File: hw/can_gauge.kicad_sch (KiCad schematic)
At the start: 28 parts, among them J1 Gauge 1, J2 Gauge 2, J3 Gauge 3, J4 Gauge 4, J5 Gauge 5, J6 Gauge 6, J7 Power & CAN, U1 PIC16F1459-IP, U2 MCP2515-xST, U3 MCP2561T-E/SN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

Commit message: hw: partial uc layout
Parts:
- removed U2: MCP2515-xST, Package_SO:TSSOP-20_4.4x6.5mm_P0.65mm, symbol Interface_CAN_LIN:MCP2515-xST
- removed U3: MCP2561T-E/SN, Package_SO:SOIC-8_3.9x4.9mm_P1.27mm, symbol Interface_CAN_LIN:MCP2561-E-SN
- added U2: ~, Package_DIP:DIP-18_W7.62mm, symbol symbols:MCP2515-xP
- added XCVR1: MCP2561-E-P, Package_DIP:DIP-8_W7.62mm, symbol Interface_CAN_LIN:MCP2561-E-P
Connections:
- net +12V: now also J7.3 (Pin_3); no longer J7.4 (Pin_4)
- net +5V: now also U2.18 (VDD), XCVR1.3 (VDD)
- net CAN_H: now also J7.2 (Pin_2), XCVR1.7 (CANH); no longer J7.1 (Pin_1)
- net CAN_L: now also J7.4 (Pin_4), XCVR1.6 (CANL); no longer J7.3 (Pin_3)
- net CLK: now also U2.8 (OSC1)
- net GND: now also J7.1 (Pin_1), U2.9 (VSS), XCVR1.2 (VSS), XCVR1.8 (STBY); no longer J7.2 (Pin_2)
- net RX: now also U2.2 (RXCAN), XCVR1.4 (RXD)
- net SCK: now also U2.13 (SCK)
- net SI: now also U2.15 (SO)
- net SO: now also U2.14 (SI)
- net TX: now also U2.1 (TXCAN), XCVR1.1 (TXD)
- net ~{CS}: now also U2.16 (~{CS})
- net ~{INT}: now also U2.12 (~{INT})
- net at R2.1: now also U2.17 (~{RESET})
- no-connect marks 10 -> 15
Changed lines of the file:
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@@
 	)
 	(no_connect
+		(at 123.19 57.15)
+	)
+	(no_connect
 		(at 123.19 41.91)
 	)
@@
 	)
 	(no_connect
+		(at 123.19 69.85)
+	)
+	(no_connect
 		(at 66.04 66.04)
 	)
 	(no_connect
+		(at 224.79 62.23)
+	)
+	(no_connect
+		(at 224.79 46.99)
+	)
+	(no_connect
 		(at 63.5 127)
 	)
 	(no_connect
+		(at 224.79 64.77)
+	)
+	(no_connect
 		(at 278.13 204.47)
 	)
@@
 	(wire
 		(pts
+			(xy 57.15 264.16) (xy 69.85 264.16)
+		)
+		(stroke
+			(width 0)
+			(type default)
+		)
+	)
+	(wire
+		(pts
 			(xy 322.58 179.07) (xy 325.12 179.07)
 		)
@@
 	(wire
 		(pts
-			(xy 57.15 261.62) (xy 63.5 261.62)
+			(xy 248.92 123.19) (xy 248.92 186.69)
 		)
 		(stroke
@@
 	(wire
 		(pts
-			(xy 248.92 123.19) (xy 248.92 186.69)
+			(xy 30.48 261.62) (xy 44.45 261.62)
 		)
 		(stroke
@@
 	(global_label "CAN_H"
 		(shape bidirectional)
-		(at 44.45 261.62 180)
+		(at 44.45 264.16 180)
 		(fields_autoplaced yes)
 		(effects
@@
 		)
 		(property "Intersheetrefs" "${INTERSHEET_REFS}"
-			(at 34.3663 261.62 0)
+			(at 34.3663 264.16 0)
 			(effects
 				(font
@@
 	(global_label "CAN_L"
 		(shape bidirectional)
-		(at 57.15 264.16 0)
+		(at 57.15 261.62 0)
 		(fields_autoplaced yes)
 		(effects
@@
 		)
 		(property "Intersheetrefs" "${INTERSHEET_REFS}"
-			(at 66.9313 264.16 0)
+			(at 66.9313 261.62 0)
 			(effects
 				(font
@@
 	)
 	(symbol
+		(lib_id "Interface_CAN_LIN:MCP2561-E-P")
+		(at 50.8 127 0)
+		(unit 1)
+		(exclude_from_sim no)
+		(in_bom yes)
+		(on_board yes)
+		(dnp no)
+		(fields_autoplaced yes)
+		(property "Reference" "XCVR1"
+			(at 52.9433 114.3 0)
+			(effects
+				(font
+					(size 1.27 1.27)
+				)
+				(justify left)
+			)
+		)
+		(property "Value" "MCP2561-E-P"
+			(at 52.9433 116.84 0)
+			(effects
+				(font
+					(size 1.27 1.27)
+				)
+				(justify left)
+			)
+		)
+		(property "Footprint" "Package_DIP:DIP-8_W7.62mm"
+			(at 50.8 139.7 0)
+			(effects
+				(font
+					(size 1.27 1.27)
+					(italic yes)
+				)
+				(hide yes)
+			)
+		)
+		(property "Datasheet" "http://ww1.microchip.com/downloads/en/DeviceDoc/25167A.pdf"
+			(at 50.8 127 0)
+			(effects
+				(font
+					(size 1.27 1.27)
+				)
+				(hide yes)
+			)
+		)
+		(property "Description" "High-Speed CAN Transceiver, 1Mbps, 5V supply, SPLIT pin, -40C to +125C, DIP-8"
+			(at 50.8 127 0)
+			(effects
+				(font
+					(size 1.27 1.27)
+				)
+				(hide yes)
+			)
+		)
+		(pin "1"
+		)
+		(pin "5"
+		)
+		(pin "3"
+		)
+		(pin "8"
+		)
+		(pin "7"
+		)
+		(pin "6"
+		)
+		(pin "2"
+		)
+		(pin "4"
+		)
+		(instances
+			(project ""
+				(path "/a1545928-1195-40b9-b3c4-78f837012afb"
+					(reference "XCVR1")
+					(unit 1)
+				)
+			)
+		)
+	)
+	(symbol
 		(lib_name "GND_8")
 		(lib_id "power:GND")
@@
 	)
 	(symbol
-		(lib_id "Interface_CAN_LIN:MCP2515-xST")
+		(lib_id "symbols:MCP2515-xP")
 		(at 50.8 55.88 0)
 		(unit 1)
@@
 		(on_board yes)
 		(dnp no)
-		(fields_autoplaced yes)
 		(property "Reference" "U2"
-			(at 52.9433 33.02 0)
+			(at 52.324 33.782 0)
 			(effects
 				(font
@@
 			)
 		)
-		(property "Value" "MCP2515-xST"
-			(at 52.9433 35.56 0)
+		(property "Value" "~"
+			(at 52.9433 34.29 0)
 			(effects
 				(font
@@
 			)
 		)
-		(property "Footprint" "Package_SO:TSSOP-20_4.4x6.5mm_P0.65mm"
-			(at 50.8 78.74 0)
+		(property "Footprint" "Package_DIP:DIP-18_W7.62mm"
+			(at 50.8 55.88 0)
 			(effects
 				(font
 					(size 1.27 1.27)
-					(italic yes)
 				)
 				(hide yes)
 			)
 		)
-		(property "Datasheet" "http://ww1.microchip.com/downloads/en/DeviceDoc/21801e.pdf"
-			(at 53.34 76.2 0)
+		(property "Datasheet" "https://ww1.microchip.com/downloads/aemDocuments/documents/APID/ProductDocuments/DataSheets/MCP2515-Family-Data-Sheet-DS20001801K.pdf"
+			(at 50.8 55.88 0)
 			(effects
 				(font
@@
 			)
 		)
-		(property "Description" "Stand-Alone CAN Controller with SPI Interface, TSSOP-20"
+		(property "Description" "CAN transceiver with SPI interface"
 			(at 50.8 55.88 0)
 			(effects
@@
 			)
 		)
-		(pin "5"
-		)
-		(pin "18"
-		)
-		(pin "20"
-		)
-		(pin "19"
-		)
-		(pin "14"
+		(pin "9"
 		)
-		(pin "7"
+		(pin "5"
 		)
 		(pin "6"
 		)
-		(pin "10"
-		)
-		(pin "3"
+		(pin "17"
 		)
-		(pin "15"
+		(pin "10"
 		)
 		(pin "12"
 		)
+		(pin "18"
+		)
 		(pin "1"
 		)
 		(pin "4"
 		)
+		(pin "11"
+		)
 		(pin "2"
 		)
-		(pin "9"
+		(pin "8"
 		)
-		(pin "11"
+		(pin "3"
 		)
-		(pin "17"
+		(pin "7"
+		)
+		(pin "13"
 		)
 		(pin "16"
 		)
-		(pin "8"
+		(pin "14"
 		)
-		(pin "13"
+		(pin "15"
 		)
 		(instances
@@
 		(lib_name "GND_5")
 		(lib_id "power:GND")
-		(at 44.45 264.16 0)
+		(at 30.48 261.62 0)
 		(unit 1)
 		(exclude_from_sim no)
@@
 		(fields_autoplaced yes)
 		(property "Reference" "#PWR09"
-			(at 44.45 270.51 0)
+			(at 30.48 267.97 0)
 			(effects
 				(font
@@
 		)
 		(property "Value" "GND"
-			(at 44.45 269.24 0)
+			(at 30.48 266.7 0)
 			(effects
 				(font
@@
 		)
 		(property "Footprint" ""
-			(at 44.45 264.16 0)
+			(at 30.48 261.62 0)
 			(effects
 				(font
@@
 		)
 		(property "Datasheet" ""
-			(at 44.45 264.16 0)
+			(at 30.48 261.62 0)
 			(effects
 				(font
@@
 		)
 		(property "Description" "Power symbol creates a global label with name \"GND\" , ground"
-			(at 44.45 264.16 0)
+			(at 30.48 261.62 0)
 			(effects
 				(font
@@
 	)
 	(symbol
-		(lib_id "Interface_CAN_LIN:MCP2561-E-SN")
-		(at 50.8 127 0)
-		(unit 1)
-		(exclude_from_sim no)
-		(in_bom yes)
-		(on_board yes)
-		(dnp no)
-		(property "Reference" "U3"
-			(at 52.9433 114.3 0)
-			(effects
-				(font
-					(size 1.27 1.27)
-				)
-				(justify left)
-			)
-		)
-		(property "Value" "MCP2561T-E/SN"
-			(at 52.9433 116.84 0)
-			(effects
-				(font
-					(size 1.27 1.27)
-				)
-				(justify left)
-			)
-		)
-		(property "Footprint" "Package_SO:SOIC-8_3.9x4.9mm_P1.27mm"
-			(at 50.8 139.7 0)
-			(effects
-				(font
-					(size 1.27 1.27)
-					(italic yes)
-				)
-				(hide yes)
-			)
-		)
-		(property "Datasheet" "https://ww1.microchip.com/downloads/en/DeviceDoc/20005167C.pdf"
-			(at 50.8 127 0)
-			(effects
-				(font
-					(size 1.27 1.27)
-				)
-				(hide yes)
-			)
-		)
-		(property "Description" "High-Speed CAN Transceiver, 1Mbps, 5V supply, SPLIT pin, -40C to +125C, SOIC-8"
-			(at 50.8 127 0)
-			(effects
-				(font
-					(size 1.27 1.27)
-				)
-				(hide yes)
-			)
-		)
-		(pin "3"
-		)
-		(pin "5"
-		)
-		(pin "7"
-		)
-		(pin "8"
-		)
-		(pin "4"
-		)
-		(pin "1"
-		)
-		(pin "6"
-		)
-		(pin "2"
-		)
-		(instances
-			(project ""
-				(path "/a1545928-1195-40b9-b3c4-78f837012afb"
-					(reference "U3")
-					(unit 1)
-				)
-			)
-		)
-	)
-	(symbol
 		(lib_id "power:GND")
 		(at 118.11 130.81 0)
@@
 		(lib_name "+12V_1")
 		(lib_id "power:+12V")
-		(at 63.5 261.62 0)
+		(at 69.85 264.16 0)
 		(unit 1)
 		(exclude_from_sim no)
@@
 		(fields_autoplaced yes)
 		(property "Reference" "#PWR08"
-			(at 63.5 265.43 0)
+			(at 69.85 267.97 0)
 			(effects
 				(font
@@
 		)
 		(property "Value" "+12V"
-			(at 63.5 256.54 0)
+			(at 69.85 259.08 0)
 			(effects
 				(font
@@
 		)
 		(property "Footprint" ""
-			(at 63.5 261.62 0)
+			(at 69.85 264.16 0)
 			(effects
 				(font
@@
 		)
 		(property "Datasheet" ""
-			(at 63.5 261.62 0)
+			(at 69.85 264.16 0)
 			(effects
 				(font
@@
 		)
 		(property "Description" "Power symbol creates a global label with name \"+12V\""
-			(at 63.5 261.62 0)
+			(at 69.85 264.16 0)
 			(effects
 				(font

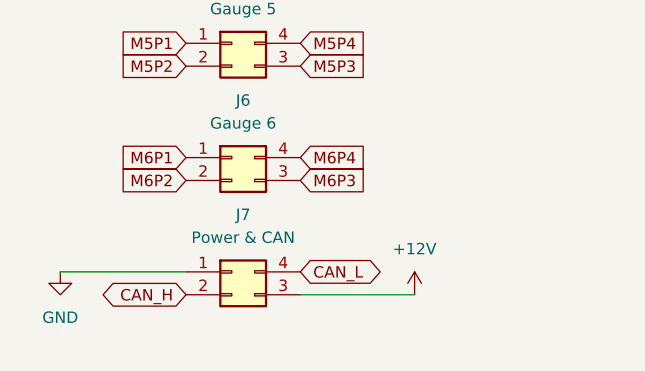
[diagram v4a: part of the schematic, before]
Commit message: hw: vreg placement
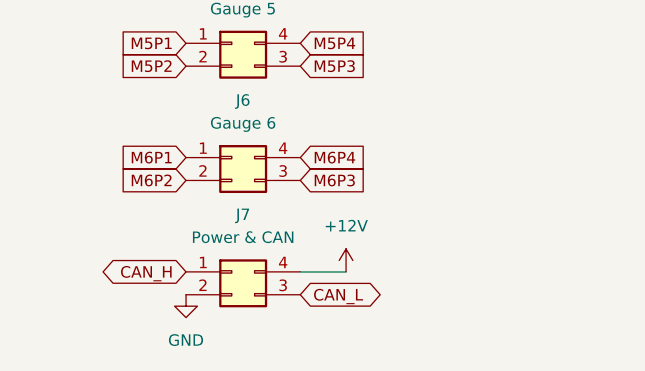
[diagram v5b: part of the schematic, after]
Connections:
- net +12V: now also J7.4 (Pin_4); no longer J7.3 (Pin_3)
- net CAN_H: now also J7.1 (Pin_1); no longer J7.2 (Pin_2)
- net CAN_L: now also J7.3 (Pin_3); no longer J7.4 (Pin_4)
- net GND: now also J7.2 (Pin_2); no longer J7.1 (Pin_1)
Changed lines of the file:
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@@
 	(wire
 		(pts
-			(xy 57.15 264.16) (xy 69.85 264.16)
-		)
-		(stroke
-			(width 0)
-			(type default)
-		)
-	)
-	(wire
-		(pts
 			(xy 322.58 179.07) (xy 325.12 179.07)
 		)
@@
 	(wire
 		(pts
-			(xy 30.48 261.62) (xy 44.45 261.62)
-		)
-		(stroke
-			(width 0)
-			(type default)
-		)
-	)
-	(wire
-		(pts
 			(xy 267.97 171.45) (xy 267.97 176.53)
 		)
@@
 	(wire
 		(pts
+			(xy 57.15 261.62) (xy 62.23 261.62)
+		)
+		(stroke
+			(width 0)
+			(type default)
+		)
+	)
+	(wire
+		(pts
 			(xy 255.27 62.23) (xy 255.27 64.77)
 		)
@@
 	(global_label "CAN_H"
 		(shape bidirectional)
-		(at 44.45 264.16 180)
+		(at 44.45 261.62 180)
 		(fields_autoplaced yes)
 		(effects
@@
 		)
 		(property "Intersheetrefs" "${INTERSHEET_REFS}"
-			(at 34.3663 264.16 0)
+			(at 34.3663 261.62 0)
 			(effects
 				(font
@@
 	(global_label "CAN_L"
 		(shape bidirectional)
-		(at 57.15 261.62 0)
+		(at 57.15 264.16 0)
 		(fields_autoplaced yes)
 		(effects
@@
 		)
 		(property "Intersheetrefs" "${INTERSHEET_REFS}"
-			(at 66.9313 261.62 0)
+			(at 66.9313 264.16 0)
 			(effects
 				(font
@@
 		(lib_name "GND_5")
 		(lib_id "power:GND")
-		(at 30.48 261.62 0)
+		(at 44.45 264.16 0)
 		(unit 1)
 		(exclude_from_sim no)
@@
 		(fields_autoplaced yes)
 		(property "Reference" "#PWR09"
-			(at 30.48 267.97 0)
+			(at 44.45 270.51 0)
 			(effects
 				(font
@@
 		)
 		(property "Value" "GND"
-			(at 30.48 266.7 0)
+			(at 44.45 269.24 0)
 			(effects
 				(font
@@
 		)
 		(property "Footprint" ""
-			(at 30.48 261.62 0)
+			(at 44.45 264.16 0)
 			(effects
 				(font
@@
 		)
 		(property "Datasheet" ""
-			(at 30.48 261.62 0)
+			(at 44.45 264.16 0)
 			(effects
 				(font
@@
 		)
 		(property "Description" "Power symbol creates a global label with name \"GND\" , ground"
-			(at 30.48 261.62 0)
+			(at 44.45 264.16 0)
 			(effects
 				(font
@@
 		(lib_name "+12V_1")
 		(lib_id "power:+12V")
-		(at 69.85 264.16 0)
+		(at 62.23 261.62 0)
 		(unit 1)
 		(exclude_from_sim no)
@@
 		(fields_autoplaced yes)
 		(property "Reference" "#PWR08"
-			(at 69.85 267.97 0)
+			(at 62.23 265.43 0)
 			(effects
 				(font
@@
 		)
 		(property "Value" "+12V"
-			(at 69.85 259.08 0)
+			(at 62.23 256.54 0)
 			(effects
 				(font
@@
 		)
 		(property "Footprint" ""
-			(at 69.85 264.16 0)
+			(at 62.23 261.62 0)
 			(effects
 				(font
@@
 		)
 		(property "Datasheet" ""
-			(at 69.85 264.16 0)
+			(at 62.23 261.62 0)
 			(effects
 				(font
@@
 		)
 		(property "Description" "Power symbol creates a global label with name \"+12V\""
-			(at 69.85 264.16 0)
+			(at 62.23 261.62 0)
 			(effects
 				(font

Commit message: hw: USB port
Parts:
- added C10: 0.1 uF, Capacitor_THT:C_Rect_L4.0mm_W2.5mm_P2.50mm, symbol Device:C_Small
- added F1: 500 mA, Fuse:Fuse_0402_1005Metric, symbol Device:Fuse_Small
- added J8: USB_B, footprints:UJ2-BH-BL1-TH, symbol Connector:USB_B
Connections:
- net +5V: now also C10.2, F1.2
- net GND: now also C10.1, J8.4 (GND), J8.5 (Shield)
- net USB+: now also U1.19 (RA0/D+/ICSPDAT), J8.3 (D+)
- net USB-: now also U1.18 (RA1/D-/ICSPCLK), J8.2 (D-)
- new net: F1.1, J8.1 (VBUS)

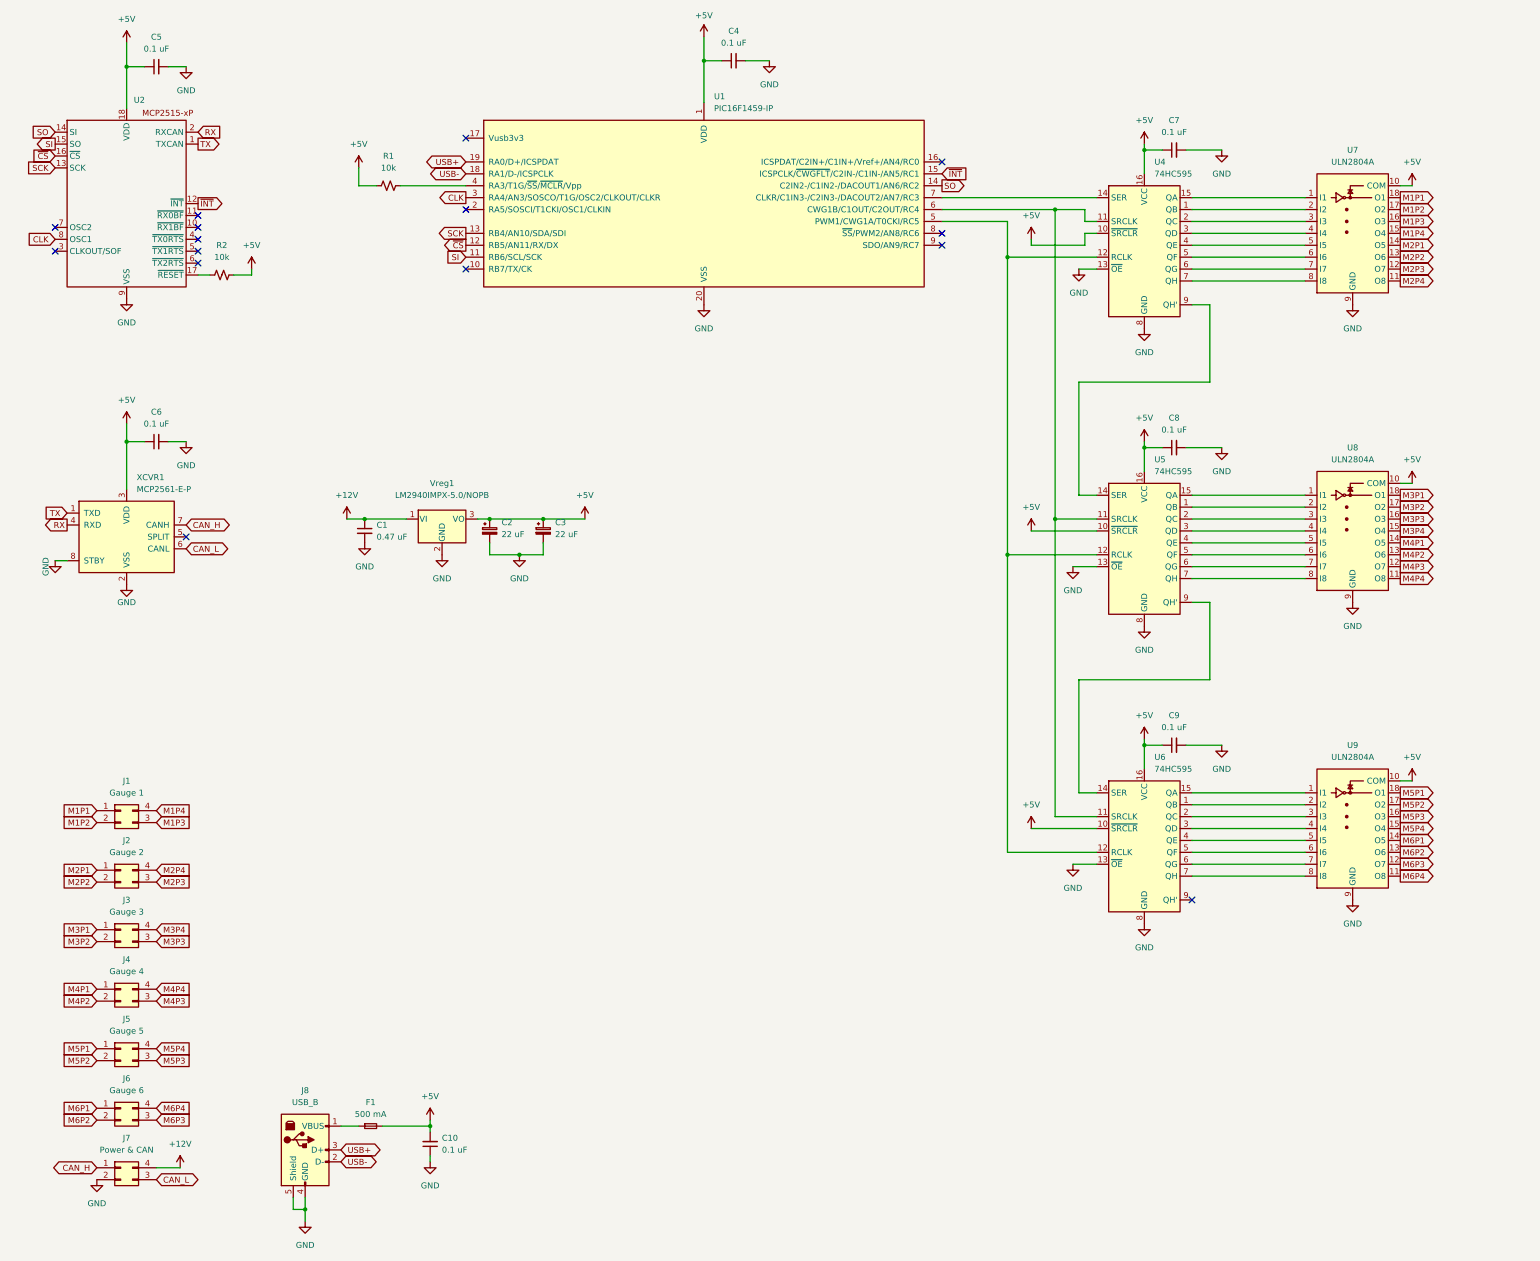
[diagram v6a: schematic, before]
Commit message: hw: generate bom and cpl
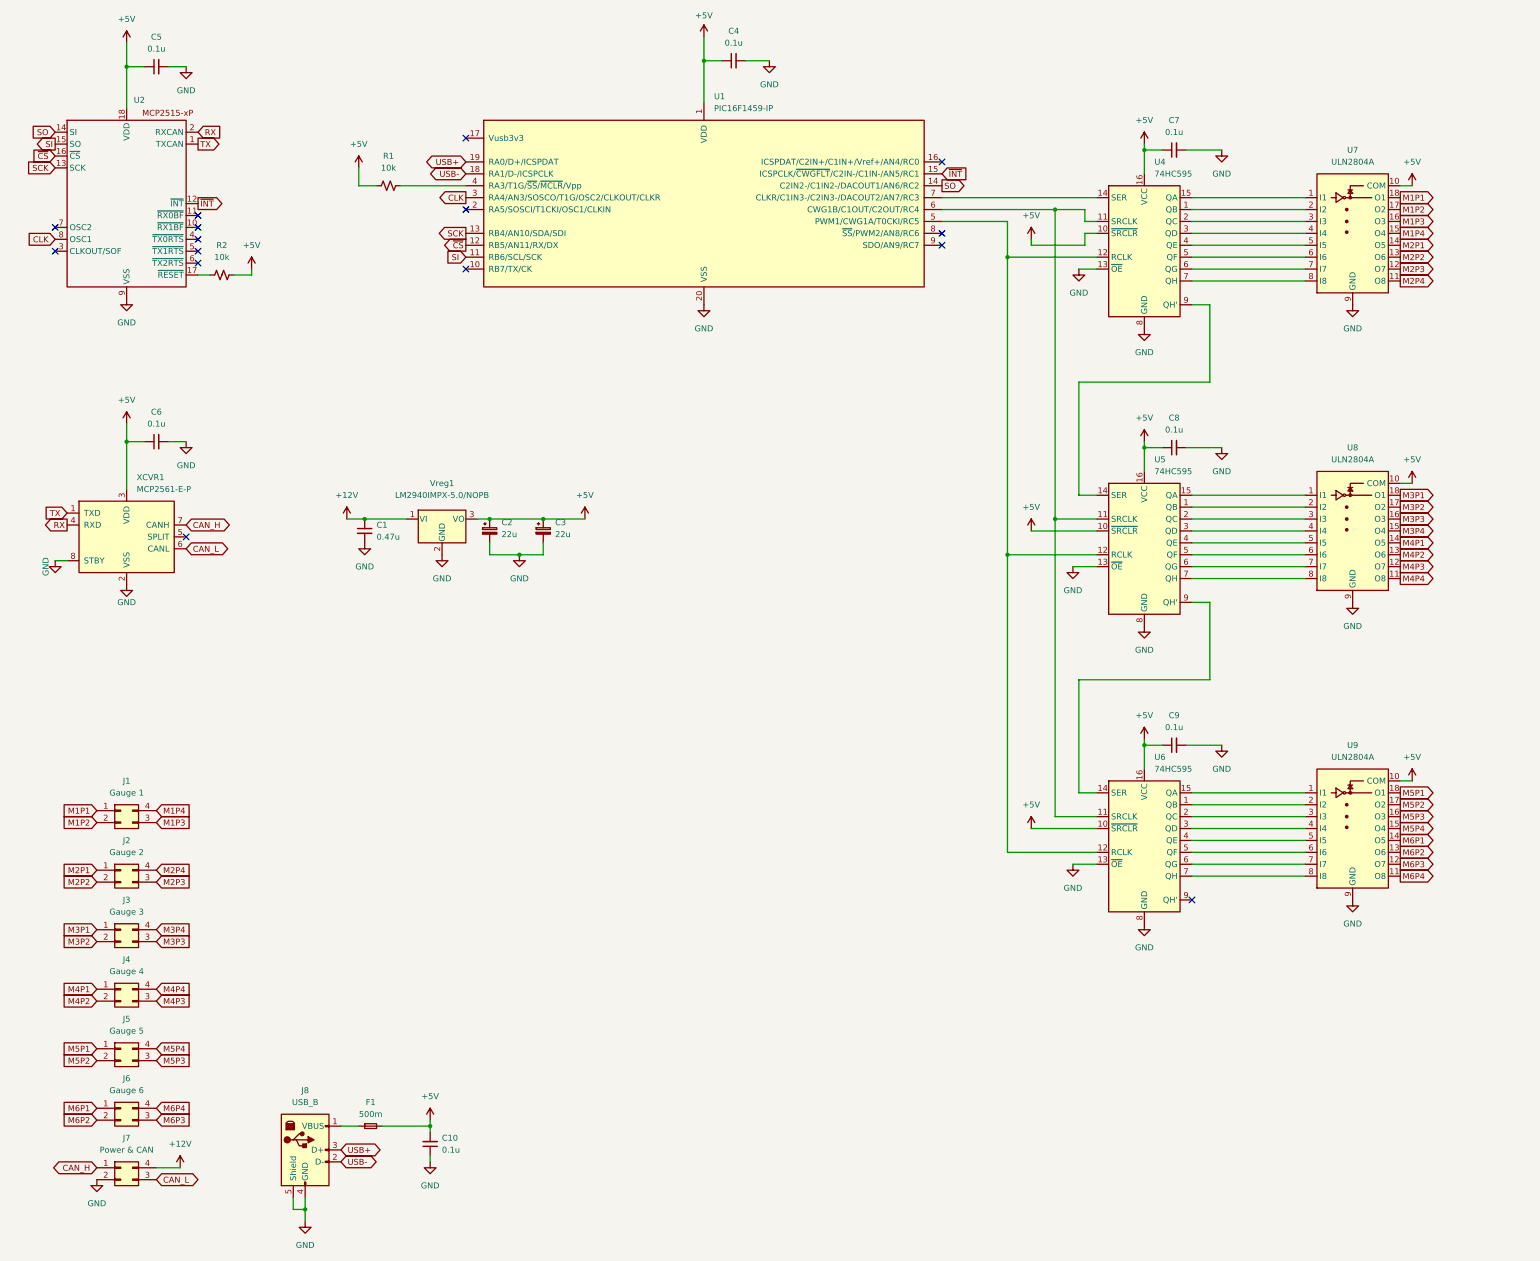
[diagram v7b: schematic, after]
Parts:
- C1: value 0.47 uF -> 0.47u
- C10, C4, C5, C6, C7, C8, C9: value 0.1 uF -> 0.1u
- C2, C3: value 22 uF -> 22u
- F1: value 500 mA -> 500m
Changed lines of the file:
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@@
 			)
 		)
-		(property "Value" "0.47 uF"
+		(property "Value" "0.47u"
 			(at 104.14 127.0062 0)
 			(effects
@@
 			)
 		)
-		(property "Value" "0.1 uF"
+		(property "Value" "0.1u"
 			(at 180.3463 21.59 90)
 			(effects
@@
 			)
 		)
-		(property "Value" "500 mA"
+		(property "Value" "500m"
 			(at 102.87 250.19 0)
 			(effects
@@
 			)
 		)
-		(property "Value" "0.1 uF"
+		(property "Value" "0.1u"
 			(at 57.1563 102.87 90)
 			(effects
@@
 			)
 		)
-		(property "Value" "0.1 uF"
+		(property "Value" "0.1u"
 			(at 57.1563 22.86 90)
 			(effects
@@
 			)
 		)
-		(property "Value" "0.1 uF"
+		(property "Value" "0.1u"
 			(at 274.3263 167.64 90)
 			(effects
@@
 			)
 		)
-		(property "Value" "0.1 uF"
+		(property "Value" "0.1u"
 			(at 118.0712 257.8035 0)
 			(effects
@@
 			)
 		)
-		(property "Value" "22 uF"
+		(property "Value" "22u"
 			(at 130.81 126.4538 0)
 			(effects
@@
 			)
 		)
-		(property "Value" "0.1 uF"
+		(property "Value" "0.1u"
 			(at 274.3263 40.64 90)
 			(effects
@@
 			)
 		)
-		(property "Value" "0.1 uF"
+		(property "Value" "0.1u"
 			(at 274.3263 104.14 90)
 			(effects
@@
 			)
 		)
-		(property "Value" "22 uF"
+		(property "Value" "22u"
 			(at 142.24 126.4538 0)
 			(effects

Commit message: hw: smd caps
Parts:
- C10, C4, C5, C6, C7, C8, C9: footprint Capacitor_THT:C_Rect_L4.0mm_W2.5mm_P2.50mm -> Capacitor_SMD:C_0402_1005Metric; Digikey https://www.digikey.ca/en/products/detail/tdk-corporation/F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 -> https://www.digikey.ca/en/products/detail/murata-electronic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
- Vreg1: Digikey (none) -> https://www.digikey.ca/en/products/detail/texas-instruments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
